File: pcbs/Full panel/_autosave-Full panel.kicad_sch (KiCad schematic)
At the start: 17 parts, among them J1 Conn_01x03_Socket, Q1 Si2319CDS, Q2 PNP, Q3 NPN

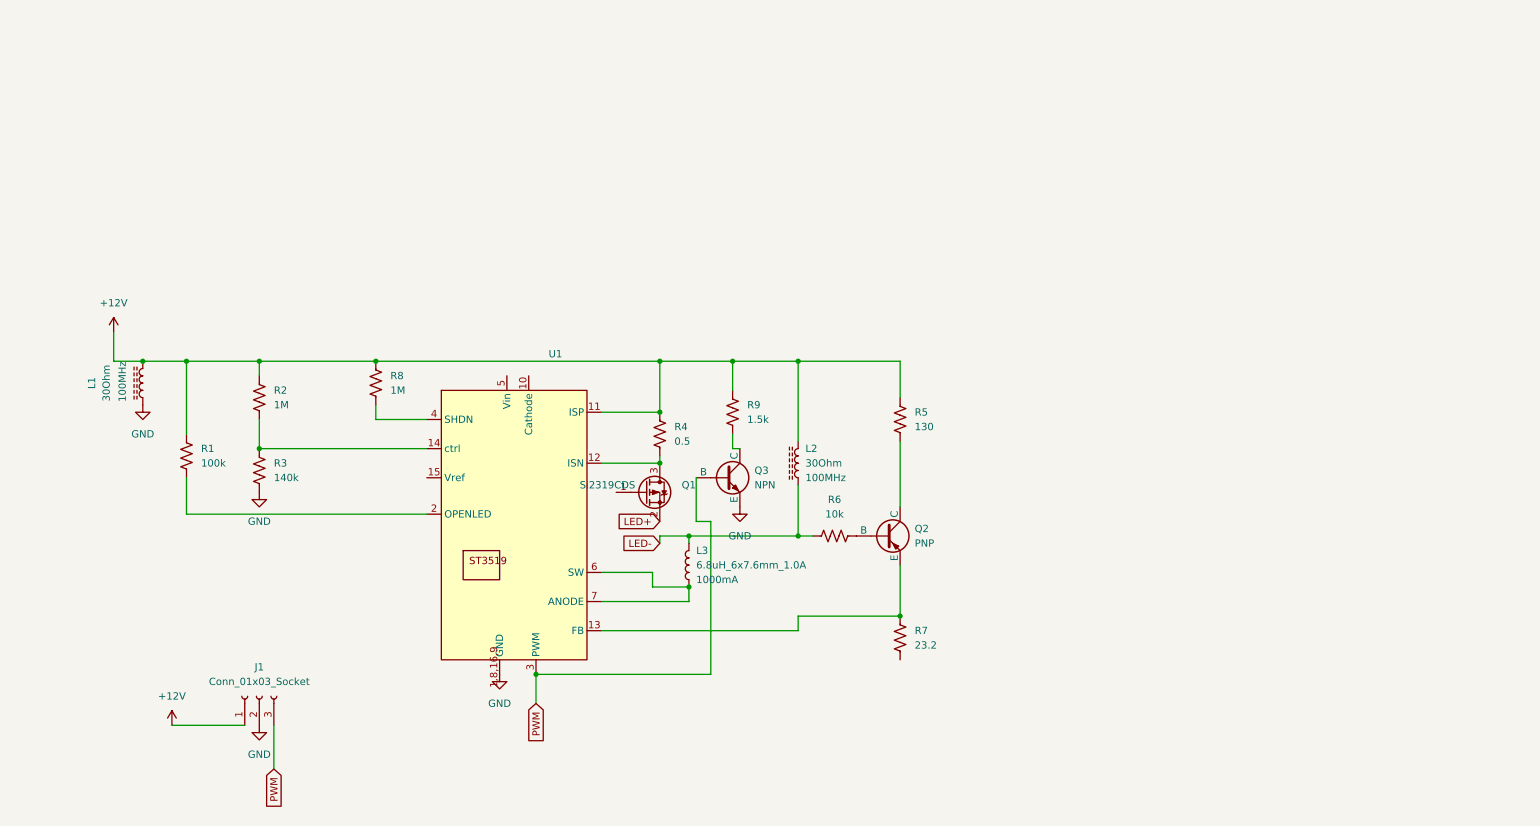
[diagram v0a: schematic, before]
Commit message: updated the full panell schematic
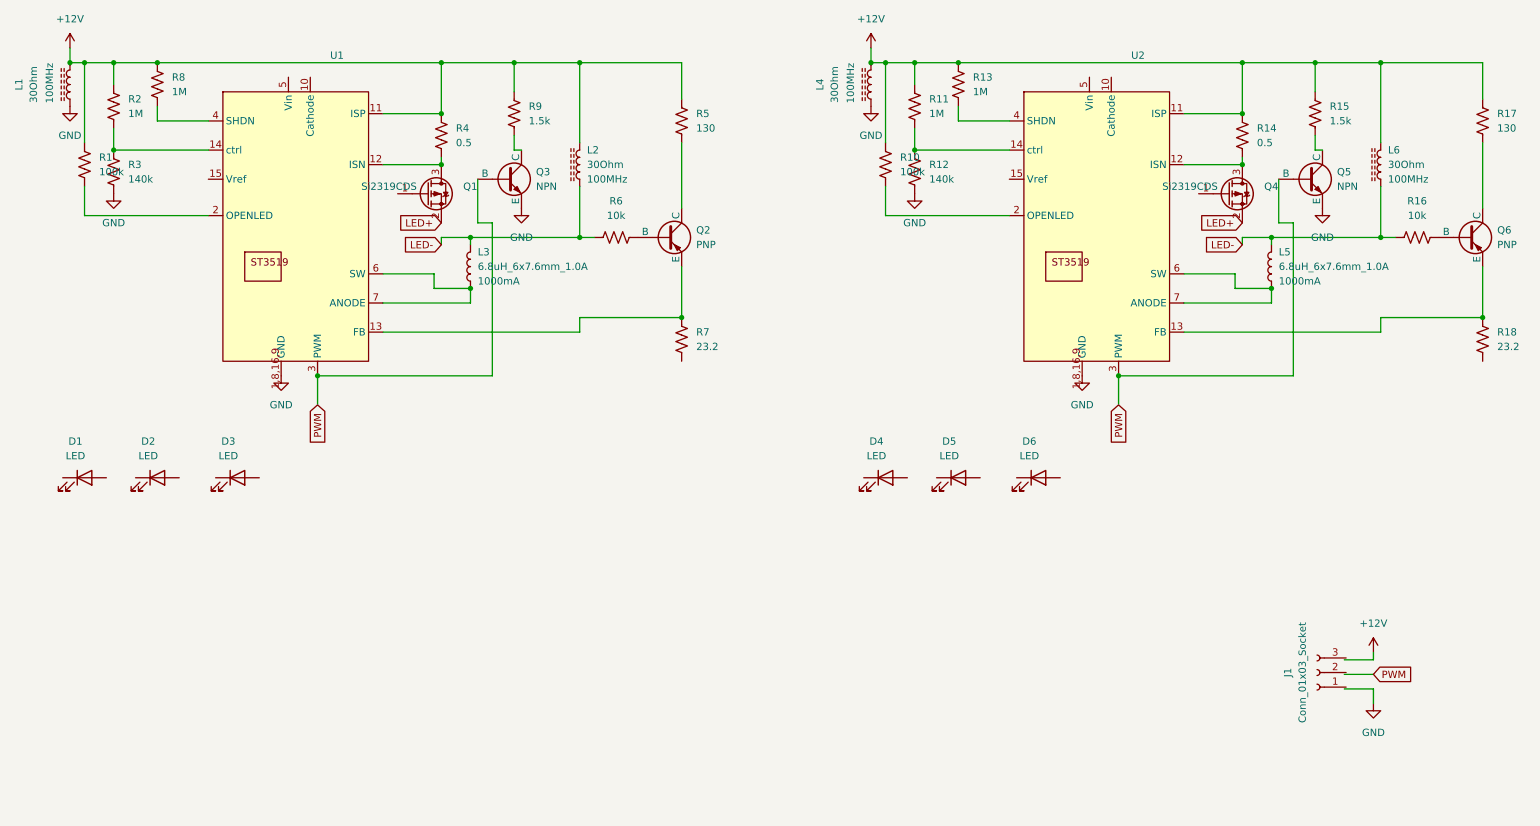
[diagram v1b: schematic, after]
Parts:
- added D1, D2, D3, D4, D5, D6: LED, symbol Device:LED
- added L4, L6: 30Ohm, SparkFun-Capacitor:C_0603_1608Metric, symbol SparkFun-Coil:30Ohm_0603_1.8A
- added L5: 6.8uH_6x7.6mm_1.0A, SparkFun-Coil:Inductor_4.7x4.7mm, symbol SparkFun-Coil:6.8uH_6x7.6mm_1.0A
- added Q4: Si2319CDS, Package_TO_SOT_SMD:SOT-23, symbol Transistor_FET:Si2319CDS
- added Q5: NPN, symbol Simulation_SPICE:NPN
- added Q6: PNP, symbol Simulation_SPICE:PNP
- added R10: 100k, SparkFun-Resistor:R_0402_1005Metric, symbol SparkFun-Resistor:100k_0402
- added R11, R13: 1M, SparkFun-Resistor:R_0402_1005Metric, symbol SparkFun-Resistor:1M_0402
- added R12: 140k, SparkFun-Resistor:R_0402_1005Metric, symbol SparkFun-Resistor:150k_0402
- added R14: 0.5, SparkFun-Resistor:R_0603_1608Metric, symbol SparkFun-Resistor:0.47_0603
- added R15: 1.5k, SparkFun-Resistor:R_0402_1005Metric, symbol SparkFun-Resistor:100_0402
- added R16: 10k, SparkFun-Resistor:R_0603_1608Metric, symbol SparkFun-Resistor:10k_0603
- added R17: 130, SparkFun-Resistor:R_0402_1005Metric, symbol SparkFun-Resistor:100_0402
- added R18: 23.2, SparkFun-Resistor:R_0603_1608Metric, symbol SparkFun-Resistor:22_0603
- added U2: ~, symbol led_driver(custom):ST3519
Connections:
- net +12V: now also L4.2, L6.2, R10.1, R11.1, R13.1, R14.1, R15.1, R17.1, U2.11 (ISP); no longer J1.1 (Pin_1)
- net GND: now also L4.1, Q5.3 (E), R12.2, U2.1,8,16,9 (GND); no longer J1.2 (Pin_2)
- net LED+: now also Q4.2 (S)
- net LED-: now also L5.2, L6.1, R16.2
- net PWM: now also Q5.2 (B), U2.3 (PWM); no longer J1.3 (Pin_3)
- new net: Q4.3 (D), R14.2, U2.12 (ISN)
- new net: Q6.2 (B), R16.1
- new net: Q5.1 (C), R15.2
- new net: Q6.1 (C), R17.2
- new net: Q6.3 (E), R18.1, U2.13 (FB)
- new net: R11.2, R12.1, U2.14 (ctrl)
- new net: R10.2, U2.2 (OPENLED)
- new net: R13.2, U2.4 (SHDN)
- new net: L5.1, U2.6 (SW), U2.7 (ANODE)
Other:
- moved on the sheet: J1, L1, L2, L3, Q1, Q2, Q3, R1, R2, R3, R4, R5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
